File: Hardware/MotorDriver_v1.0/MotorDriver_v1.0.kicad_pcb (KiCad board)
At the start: 2 copper layers, 100 x 100 mm, 4 parts

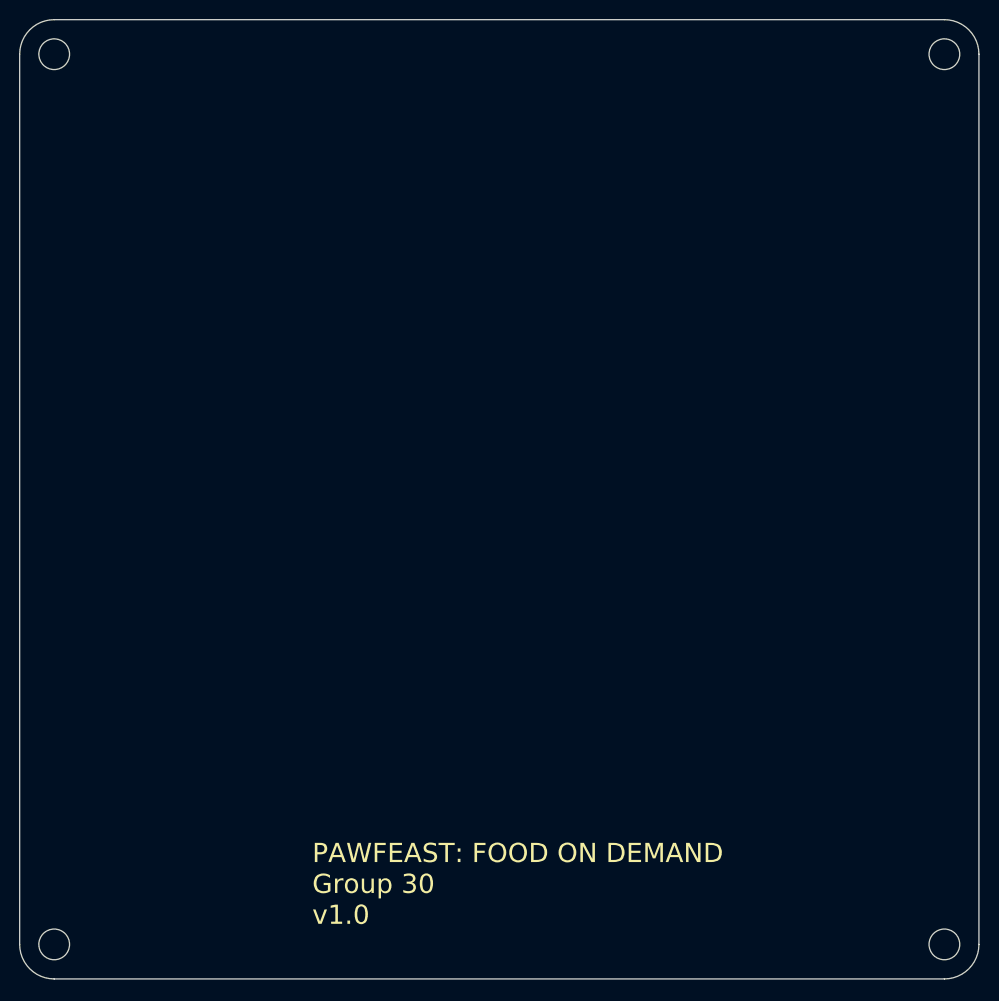
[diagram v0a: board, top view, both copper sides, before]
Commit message: updated motor driver
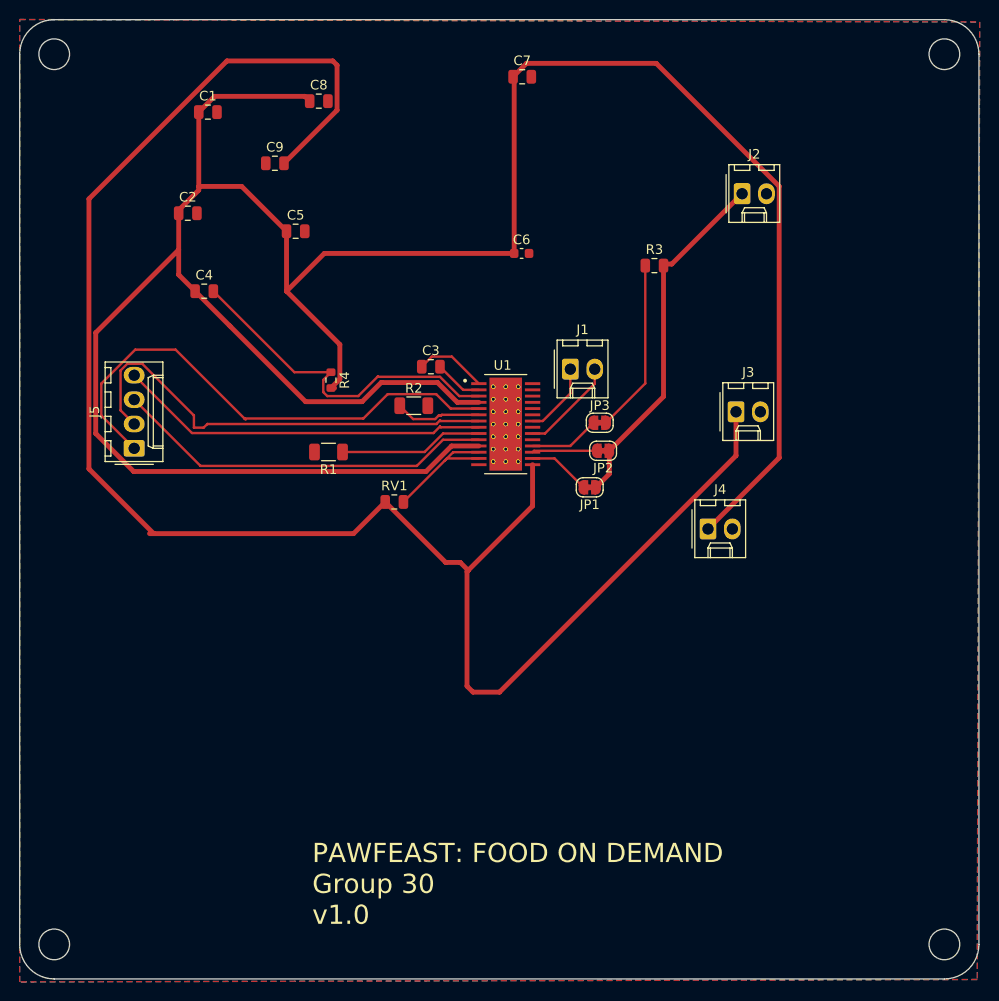
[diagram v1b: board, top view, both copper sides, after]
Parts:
- added C1: 33uF, Capacitor_SMD:C_0805_2012Metric, F.Cu at (105.5, 37.8)
- added C2: 33uF, Capacitor_SMD:C_0805_2012Metric, F.Cu at (103.4, 48.4)
- added C3: 10uF, Capacitor_SMD:C_0805_2012Metric, F.Cu at (128.7, 64.4)
- added C4: 0.1uF, Capacitor_SMD:C_0805_2012Metric, F.Cu at (105.1, 56.5)
- added C5: 33uF, Capacitor_SMD:C_0805_2012Metric, F.Cu at (114.6, 50.3)
- added C6: 4.7uF, Capacitor_SMD:C_0603_1608Metric, F.Cu at (138.2, 52.6)
- added C7: 0.1uF, Capacitor_SMD:C_0805_2012Metric, F.Cu at (138.2, 34.2)
- added C8: 0.1uF, Capacitor_SMD:C_0805_2012Metric, F.Cu at (117.0, 36.7)
- added C9: 0.47uF, Capacitor_SMD:C_0805_2012Metric, F.Cu at (112.5, 43.2)
- added J1: Conn_01x02, Connector_Molex:Molex_KK-254_AE-6410-02A_1x02_P2.54mm_Vertical, F.Cu at (143.3, 64.6)
- added J2: Conn_01x02, Connector_Molex:Molex_KK-254_AE-6410-02A_1x02_P2.54mm_Vertical, F.Cu at (161.2, 46.4)
- added J3: Conn_01x02, Connector_Molex:Molex_KK-254_AE-6410-02A_1x02_P2.54mm_Vertical, F.Cu at (160.5, 69.1)
- added J4: Conn_01x02, Connector_Molex:Molex_KK-254_AE-6410-02A_1x02_P2.54mm_Vertical, F.Cu at (157.6, 81.3)
- added J5: Conn_01x04, Connector_Molex:Molex_KK-254_AE-6410-04A_1x04_P2.54mm_Vertical, F.Cu at (97.8, 72.9)
- added JP1: SolderJumper_2_Bridged, Jumper:SolderJumper-2_P1.3mm_Bridged_RoundedPad1.0x1.5mm, F.Cu at (145.3, 77.0)
- added JP2: SolderJumper_2_Bridged, Jumper:SolderJumper-2_P1.3mm_Bridged_RoundedPad1.0x1.5mm, F.Cu at (146.7, 73.2)
- added JP3: SolderJumper_2_Bridged, Jumper:SolderJumper-2_P1.3mm_Bridged_RoundedPad1.0x1.5mm, F.Cu at (146.3, 70.2)
- added R1: 0.10, Resistor_SMD:R_1206_3216Metric, F.Cu at (118.0, 73.3)
- added R2: 0.10, Resistor_SMD:R_1206_3216Metric, F.Cu at (126.9, 68.5)
- added R3: 10k, Capacitor_SMD:C_0805_2012Metric, F.Cu at (152.0, 53.8)
- added R4: 1M, Resistor_SMD:R_0603_1608Metric, F.Cu at (118.3, 65.8)
- added RV1: 10k, Capacitor_SMD:C_0805_2012Metric, F.Cu at (124.9, 78.5)
- added U1: DRV8825PWPR, DRV8825:IC_TPS61196PWPRQ1, F.Cu at (136.5, 70.4)
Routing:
- net +12V: track 0.00 -> 280.9 mm
- net +3V3: track 0.00 -> 188.8 mm
- net Net-(J5-Pin_1): track 0.00 -> 53.8 mm
- net Net-(J5-Pin_2): track 0.00 -> 47.7 mm
- net Net-(J5-Pin_3): track 0.00 -> 39.9 mm
- net Net-(J5-Pin_4): track 0.00 -> 38.7 mm
- net +5V: track 0.00 -> 37.3 mm
- net Net-(U1-VCP): track 0.00 -> 36.3 mm
- net Net-(JP3-B): track 0.00 -> 18.1 mm
- net Net-(U1-ISENB): track 0.00 -> 15.0 mm
- net Net-(U1-AVREF): track 0.00 -> 13.6 mm
- net /DIR: track 0.00 -> 10.1 mm
- net Net-(U1-ISENA): track 0.00 -> 9.01 mm
- net /STP: track 0.00 -> 7.66 mm
- net Net-(U1-CP1): track 0.00 -> 7.55 mm
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- added copper zone on B.Cu, net GND
- added copper zone on F.Cu, net GND
